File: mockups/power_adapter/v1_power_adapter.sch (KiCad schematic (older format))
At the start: 20 parts, among them J1 Barrel_Jack, J2 Conn_02x07_Odd_Even, U1 L7805, U2 LT1963EQ, U3 LT1963EQ

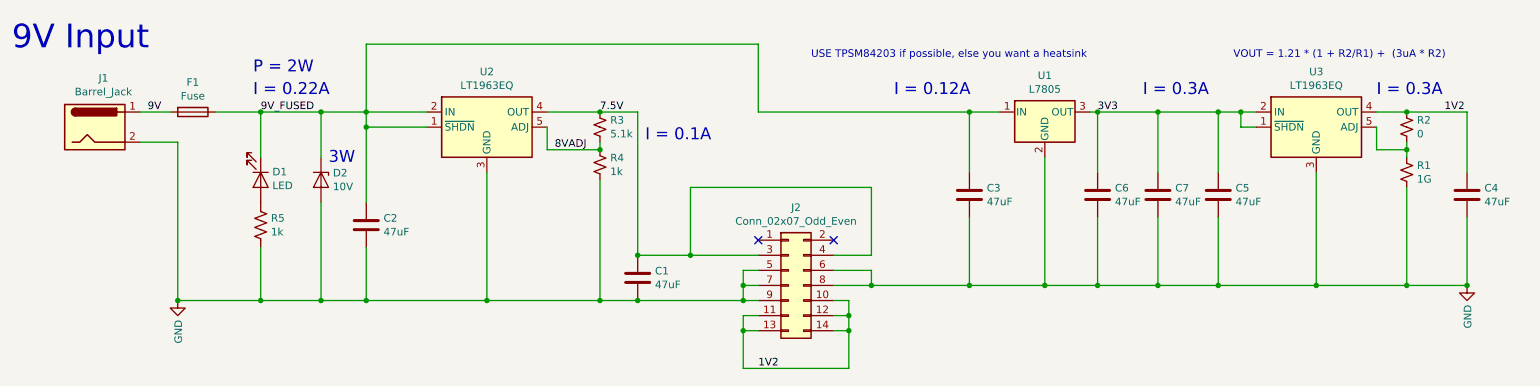
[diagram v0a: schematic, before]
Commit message: Add jumpers for current measurement
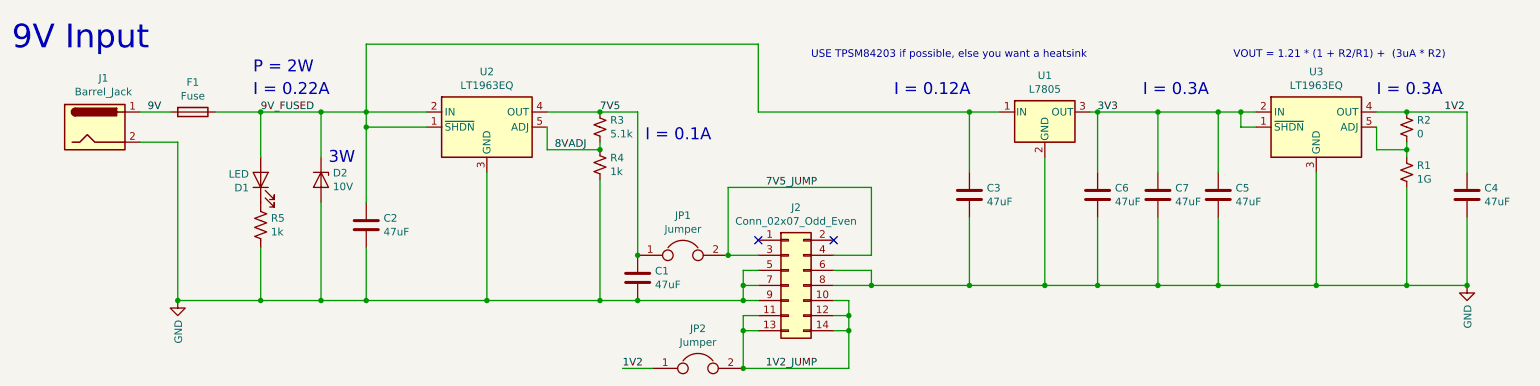
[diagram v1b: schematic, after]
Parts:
- added JP1, JP2: Jumper, Connector_PinHeader_2.54mm:PinHeader_1x02_P2.54mm_Vertical, symbol Device:Jumper
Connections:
- net 1V2: now also JP2.1; no longer J2.10 (Pin_10), J2.11 (Pin_11), J2.12 (Pin_12), J2.13 (Pin_13), J2.14 (Pin_14)
- net 9V_FUSED: now also D1.2 (A); no longer D1.1 (K)
- net at R5.1: now also D1.1 (K); no longer D1.2 (A)
- net 7.5V renamed 7V5
- net 7V5: now also JP1.1; no longer J2.3 (Pin_3), J2.4 (Pin_4)
- new net 1V2_JUMP: J2.10 (Pin_10), J2.11 (Pin_11), J2.12 (Pin_12), J2.13 (Pin_13), J2.14 (Pin_14), JP2.2
- new net 7V5_JUMP: J2.3 (Pin_3), J2.4 (Pin_4), JP1.2
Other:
- moved on the sheet: D1
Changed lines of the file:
@@
 $EndComp
 Wire Wire Line
-	5350 4000 5350 3550
-Wire Wire Line
-	5350 3550 6550 3550
+	5600 4000 5600 3550
+Wire Wire Line
+	5600 3550 6550 3550
 Wire Wire Line
 	6550 3550 6550 4000
 Wire Wire Line
 	6550 4000 6300 4000
-Connection ~ 5350 4000
-Wire Wire Line
-	5350 4000 5800 4000
 Wire Wire Line
 	5800 4100 5700 4100
@@
 Wire Wire Line
 	5700 4500 5700 4400
-Wire Wire Line
-	5000 4000 5350 4000
-Text Label 5800 4750 0    50   ~ 0
+Text Label 4900 4750 0    50   ~ 0
 1V2
 Wire Wire Line
@@
 F 4 "LTST-C193KRKT-5A" H 2500 3500 50  0001 C CNN "PN"
 	1    2500 3500
-	0    1    1    0
+	0    -1   -1   0
 $EndComp
 Wire Wire Line
@@
 Connection ~ 4000 4300
 Text Label 4750 3050 0    50   ~ 0
-7.5V
+7V5
 Text Label 1750 3050 0    50   ~ 0
 9V
@@
 Wire Wire Line
 	5800 3050 7200 3050
-Connection ~ 5000 4000
 Connection ~ 5000 4300
 Wire Wire Line
@@
 Wire Wire Line
 	8450 4200 8850 4200
+$Comp
+L Device:Jumper JP2
+U 1 1 6102B890
+P 5400 4750
+F 0 "JP2" H 5400 5014 50  0000 C CNN
+F 1 "Jumper" H 5400 4923 50  0000 C CNN
+F 2 "Connector_PinHeader_2.54mm:PinHeader_1x02_P2.54mm_Vertical" H 5400 4750 50  0001 C CNN
+F 3 "~" H 5400 4750 50  0001 C CNN
+	1    5400 4750
+	1    0    0    -1
+$EndComp
+Connection ~ 5700 4750
+Wire Wire Line
+	5100 4750 4900 4750
+$Comp
+L Device:Jumper JP1
+U 1 1 6103922F
+P 5300 4000
+F 0 "JP1" H 5300 4264 50  0000 C CNN
+F 1 "Jumper" H 5300 4173 50  0000 C CNN
+F 2 "Connector_PinHeader_2.54mm:PinHeader_1x02_P2.54mm_Vertical" H 5300 4000 50  0001 C CNN
+F 3 "~" H 5300 4000 50  0001 C CNN
+	1    5300 4000
+	1    0    0    -1
+$EndComp
+Connection ~ 5000 4000
+Connection ~ 5600 4000
+Wire Wire Line
+	5600 4000 5800 4000
+Text Label 5850 4750 0    50   ~ 0
+1V2_JUMP
+Text Label 5850 3550 0    50   ~ 0
+7V5_JUMP
 $EndSCHEMATC
